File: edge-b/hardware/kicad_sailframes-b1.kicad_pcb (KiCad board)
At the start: 2 copper layers, 79.3 x 73.9 mm, 78 parts, among them J10 I2C_EXP1, J11 I2C_EXP2, J12 I2C_EXP3, J13 GPIO_EXP, J14 UART_DBG, J15 J_AUX, J2 JST_PH_BAT, J3 U.FL, J5 MICROSD, J8 BNO085_SOCKET, J9 HOSYOND_3.5_TFT, U1 LC29HEAMD, U2 TP4056, U3 MT3608, U4 ESP32_DEVKIT_V1

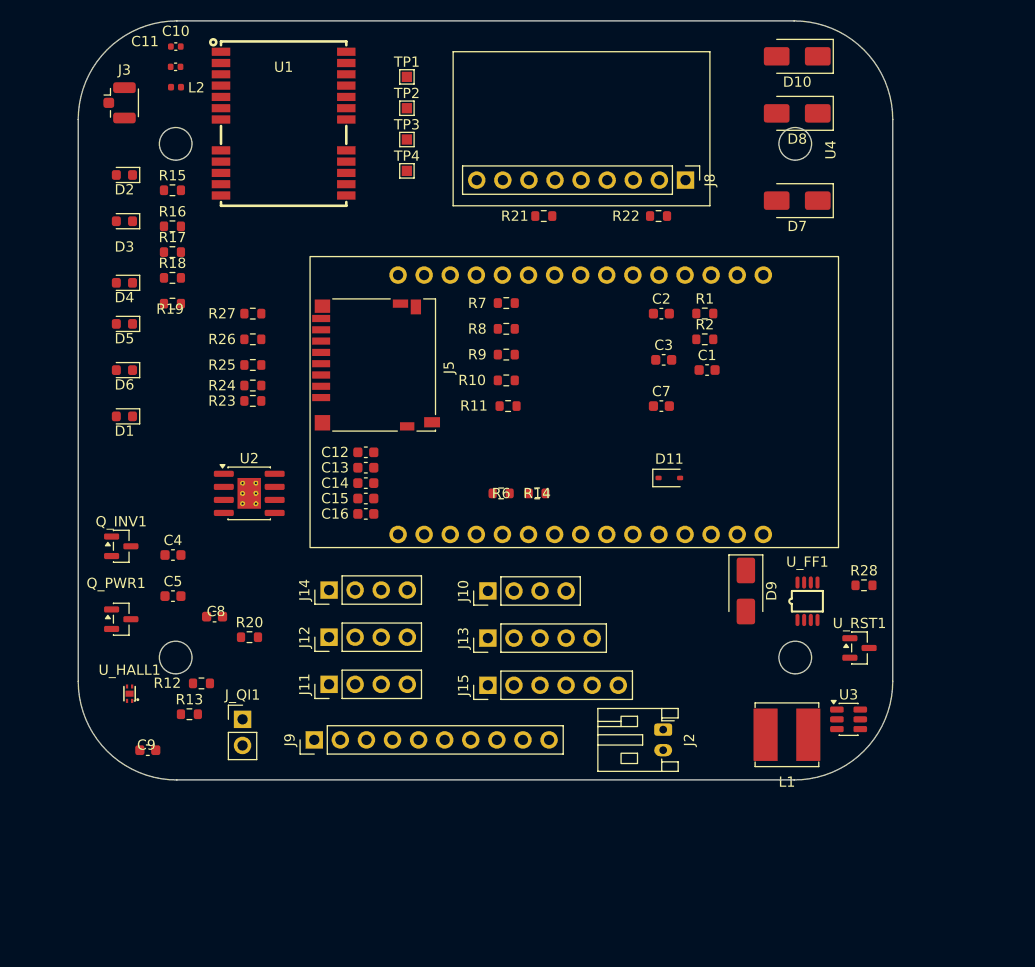
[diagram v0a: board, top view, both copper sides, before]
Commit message: B1 J_QI1: convert from THT connector to direct solder pads for Qi receiver wires
The Qi receiver module (coil + rectifier PCB) has 2 bare wire leads
(red V_QI / black GND). User decided to solder them directly into
plated through-holes on the B1 PCB rather than via a pin header.

PCB changes (J_QI1 footprint kept, geometry tweaked for wire soldering):
  - Pad 1 (V_QI):  1.7x1.7mm → 3.0x3.0mm,  drill 1.0 → 1.2mm
  - Pad 2 (GND):   1.7x1.7mm → 3.0x3.0mm,  drill 1.0 → 1.2mm
  - Pin spacing:   2.54mm → 4.0mm (better wire clearance)
  - Pad 1 stays rect (visual + polarity indicator for V_QI / red wire)
  - Pad 2 is circle
  - 1.2mm drill comfortably fits 22-24 AWG stripped wire with flux room
  - 3mm pads give good solder fillet for strain relief
  - Attribute marked: exclude_from_bom + dnp
    → JLCPCB will drill the holes but NOT install a connector

Schematic changes (J_QI1 symbol):
  - dnp: no → yes
  - in_bom: yes → no
  - in_pos_files: yes → no
  Symbol stays in schematic for documentation, but BOM and CPL
  exports will skip it.

Result: 2 plated through-holes (1.2mm diameter, 3mm pads, 4mm apart)
on F.Cu with no connector body. Hand-solder Qi receiver wires
directly into them after PCB arrives.
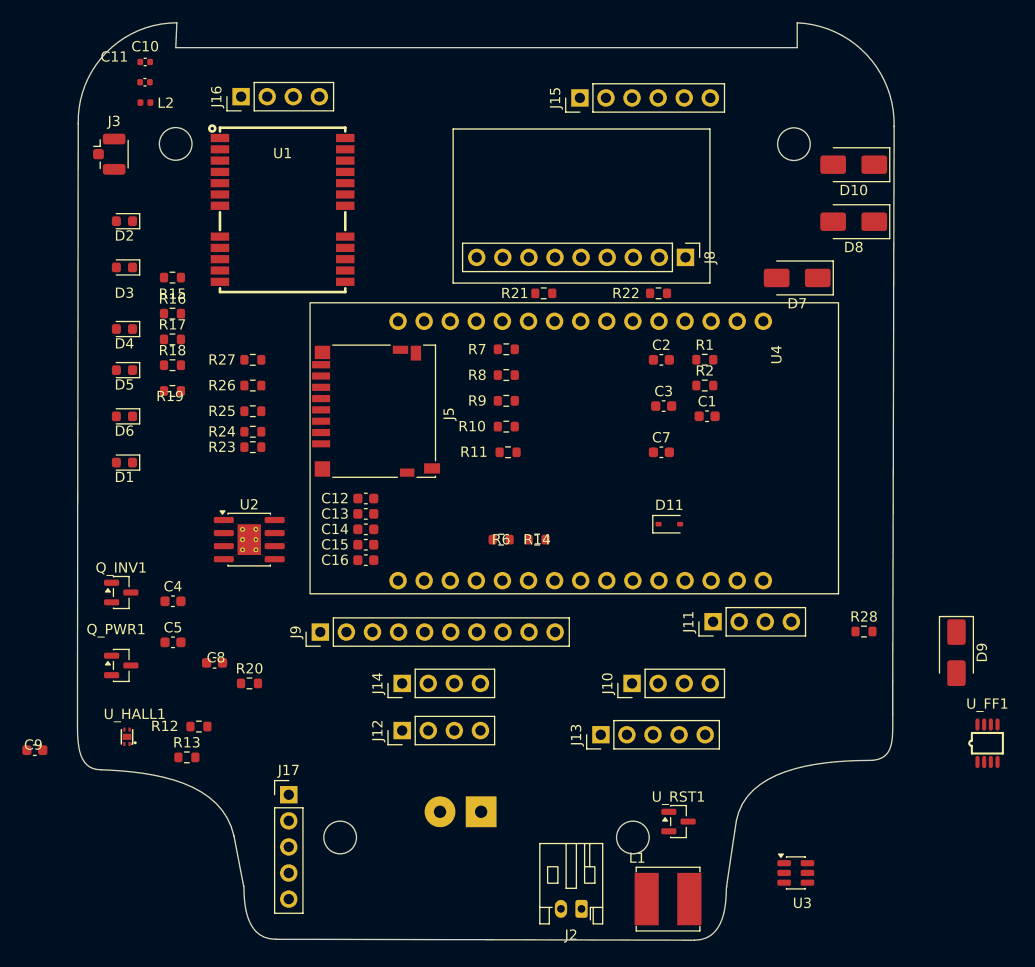
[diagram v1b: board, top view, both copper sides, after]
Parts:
- removed TP1: GNSS_TXD, TestPoint:TestPoint_Pad_1.0x1.0mm
- removed TP2: GNSS_RXD, TestPoint:TestPoint_Pad_1.0x1.0mm
- removed TP3: GNSS_RESET_N, TestPoint:TestPoint_Pad_1.0x1.0mm
- removed TP4: GND, TestPoint:TestPoint_Pad_1.0x1.0mm
- added J16: GNSS_DBG, Connector_PinHeader_2.54mm:PinHeader_1x04_P2.54mm_Vertical, F.Cu at (115.9, 72.4)
- added J17: LATCH_DBG, Connector_PinHeader_2.54mm:PinHeader_1x05_P2.54mm_Vertical, F.Cu at (120.5, 140.3)
- J_QI1: moved to B.Cu
- moved J15 57.9 mm to (148.8, 72.5)
- moved J11 37.9 mm to (161.8, 123.5)
- moved J_QI1 24.9 mm to (139.2, 142.0), turned to 90 degrees
- moved U_RST1 24.4 mm to (158.4, 142.9)
- moved U_FF1 22.3 mm to (188.5, 135.3)
- moved D9 21.4 mm to (185.5, 126.5)
- moved L1 19.7 mm to (157.4, 150.5)
- moved J2 19.2 mm to (149.0, 151.4), turned to 180 degrees
- moved J10 16.7 mm to (153.9, 129.5)
- moved U3 15.8 mm to (169.9, 147.9)
- moved J13 14.5 mm to (150.9, 134.5)
- moved D10 11.9 mm to (175.5, 79.0)
- moved D8 11.9 mm to (175.5, 84.5)
- moved J12 11.5 mm to (131.5, 134.1)
- moved J14 11.5 mm to (131.5, 129.5)
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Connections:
- U4 pad 1: unconnected-(U4-EN-Pad1) -> /EN
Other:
- board size 79.3 x 73.9 mm -> 79.5 x 89.3 mm
